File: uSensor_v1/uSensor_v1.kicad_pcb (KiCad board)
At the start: 2 copper layers, 137.6 x 77.4 mm, 287 parts, among them J1 +12V Supply, J2 Conn_01x03, J3 Conn_01x03, J4 NS25-W8P 6-pin 2,54mm, J5 USB_B, J6 GNDA-GNDD Jumper, J7 Barrel_Jack_Switch, Q1 BC817-25, Q2 BC817-25, Q3 BC847PN-7-F, Q4 BC847PN-7-F, SW1 SW_Push, SW2 SW_Push, SW3 SW_Push, U1 AM10TW-2405DZ, U10 KSS-213 Connector, U11 AD7795, U12 AD5667, U13 TBD, U14 TBD, U15 REF192, U16 TBD, U17 TBD, U2 LD1117A, U22 RCLAMP, U3 STM32F407VGTx, U4 MCP9700AT, U5 MCP9700AT, U6 LM6132A, U7 MCP9700AT, U8 MCP9700AT, U9 UG-2864KSWLG01

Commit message: Layout correction in progress.
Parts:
- added L5: 10u, Inductor_SMD:L_1210_3225Metric_Pad1.42x2.65mm_HandSolder, F.Cu at (46.9, 45.9)
- added L6: 10u, Inductor_SMD:L_1210_3225Metric_Pad1.42x2.65mm_HandSolder, F.Cu at (5.04, 47.6)
- J4: value NS25-W8P 6-pin 2,54mm -> NS25-W8P 8-pin 2,54mm; footprint Connector_Molex:Molex_KK-254_AE-6410-06A_1x06_P2.54mm_Vertical -> Connector_Molex:Molex_KK-254_AE-6410-08A_1x08_P2.54mm_Vertical
- moved C18 28.7 mm to (24.6, 35.2), turned to 90 degrees
- moved TP96 10.3 mm to (54.2, 37.2)
- moved R75 4.87 mm to (24.6, 39.0)
- moved C17 2.38 mm to (45.2, 60.6), turned to 270 degrees
- moved J4 2.32 mm to (17.1, 65.9)
- moved J5 2.00 mm to (28.5, 77.8)
- moved TP97 1.84 mm to (21.2, 33.8)
- moved C3 1.80 mm to (22.5, 45.3), turned to 270 degrees
- moved C2 1.80 mm to (16.1, 33.0)
- moved U2 1.80 mm to (17.5, 40.2)
- moved C5 1.66 mm to (45.2, 53.4), turned to 270 degrees
- moved C16 1.42 mm to (45.2, 49.2), turned to 270 degrees
- moved C4 1.35 mm to (45.2, 57.0), turned to 270 degrees
- moved C7 1.27 mm to (27.2, 44.4), turned to 180 degrees
- moved C6 1.27 mm to (40.6, 44.4), turned to 0 degrees
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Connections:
- C16 pad 1: +3V3 -> Net-(C16-Pad1)
- C16 pad 2: GNDD -> GNDA
- C38 pad 1: +3V3 -> Net-(C38-Pad1)
- C38 pad 2: GNDD -> GNDA
- C39 pad 1: +3V3 -> Net-(C38-Pad1)
- C39 pad 2: GNDD -> GNDA
- R71 pad 1: GNDD -> GNDA
- U12 pad 3: GNDD -> GNDA
- U12 pad 9: +3V3 -> Net-(C38-Pad1)
- U3 pad 20: GNDD -> GNDA
- U3 pad 22: +3V3 -> Net-(C16-Pad1)
- U3 pad 55: Net-(U3-Pad55) -> UC_DEBUG_TX
- U3 pad 56: Net-(U3-Pad56) -> UC_DEBUG_RX
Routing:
- net +3V3: track 272.1 -> 352.0 mm, vias 22 -> 14
- net GNDA: track 25.4 -> 0.00 mm, vias 0 -> 8
- net UC_DEBUG_TX: track 0.00 -> 11.0 mm
- net UC_DEBUG_RX: track 0.00 -> 10.1 mm
- net USB_VBUS: track 29.9 -> 21.3 mm
- net Net-(C16-Pad1): track 0.00 -> 6.69 mm
- net +5V: track 539.2 -> 545.0 mm
- net Net-(J5-Pad2): track 4.03 -> 0.11 mm
- net DAC_~LDAC: track 85.9 -> 82.8 mm
- net DAC_SCL: track 59.0 -> 56.3 mm
- net Net-(J5-Pad3): track 10.5 -> 8.50 mm
- net DAC_SDA: track 57.8 -> 55.8 mm
- net LCD_SCK: track 68.7 -> 70.3 mm
- net LCD_CS: track 73.0 -> 74.6 mm
- net LCD_A0: track 71.1 -> 72.7 mm
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
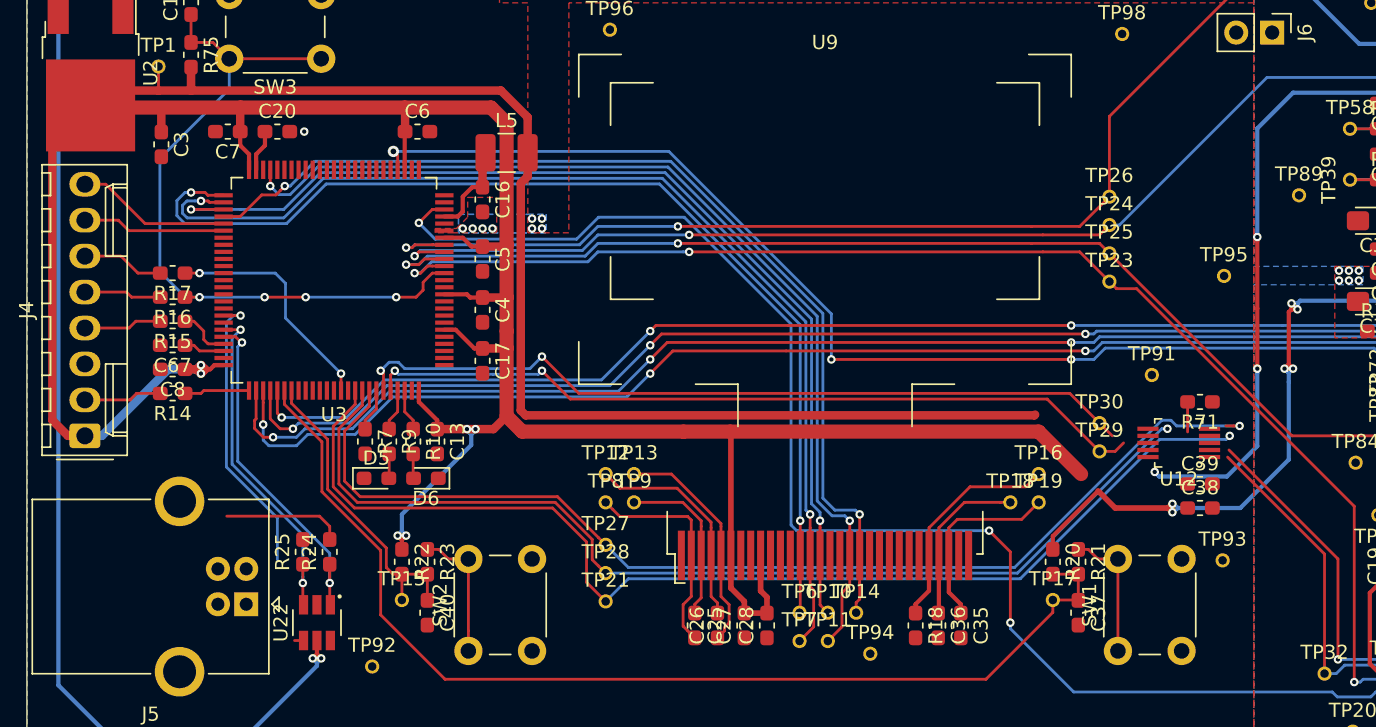
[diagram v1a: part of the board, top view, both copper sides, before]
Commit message: Layout in progress: before DAC connection changing.
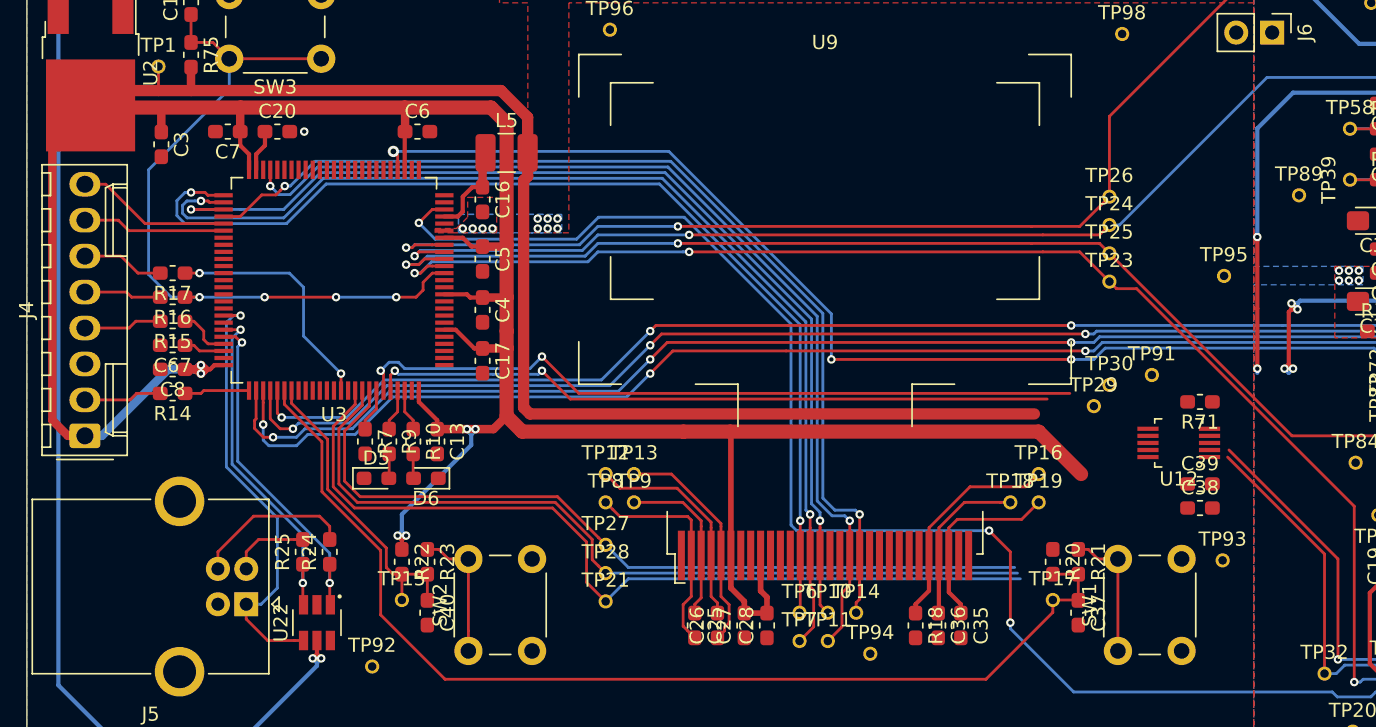
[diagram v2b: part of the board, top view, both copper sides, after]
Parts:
- moved TP29 3.22 mm to (88.4, 63.8)
- moved TP30 2.79 mm to (89.5, 62.3)
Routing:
- net +3V3: track 352.0 -> 322.2 mm, vias 14 -> 12
- net DAC_~CLR: track 78.4 -> 57.0 mm, vias 1 -> 0
- net DAC_~LDAC: track 82.8 -> 61.7 mm, vias 1 -> 0
- net DAC_ADDR: track 73.5 -> 58.7 mm, vias 1 -> 0
- net REF_2.5V: track 177.5 -> 164.1 mm, vias 4 -> 3
- net USB_VBUS: track 21.3 -> 31.0 mm
- net DAC_SDA: track 55.8 -> 48.7 mm
- net Net-(J5-Pad2): track 0.11 -> 5.67 mm
- net DAC_SCL: track 56.3 -> 52.0 mm
- net Net-(J5-Pad3): track 8.50 -> 11.4 mm
- net PROG_~RST: track 51.6 -> 52.9 mm
- net PROG_SWO: track 16.6 -> 17.2 mm
- net GNDA: vias 8 -> 10

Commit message: Layout correction in progress.
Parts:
- moved L6 143.9 mm to (144.1, 84.8), turned to 180 degrees
- moved TP29 57.7 mm to (132.8, 100.6), turned to 90 degrees
- moved TP30 56.0 mm to (131.3, 99.5), turned to 90 degrees
- moved TP91 51.7 mm to (130.6, 96.5), turned to 90 degrees
- moved C38 46.9 mm to (140.8, 84.7), turned to 90 degrees
- moved C39 45.9 mm to (139.1, 84.7), turned to 90 degrees
- moved U12 44.2 mm to (134.1, 85.8), turned to 0 degrees
- moved R71 39.4 mm to (129.1, 84.8), turned to 270 degrees
- moved TP32 33.4 mm to (135.8, 94.9)
- moved TP20 22.1 mm to (126.8, 96.1)
- moved TP77 9.34 mm to (109.4, 78.9)
- moved TP73 6.77 mm to (118.0, 82.2)
- moved TP87 6.55 mm to (149.1, 88.9)
- moved TP21 3.00 mm to (53.9, 80.6)
- moved TP27 3.00 mm to (53.9, 76.6)
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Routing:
- net +3V3: track 322.2 -> 417.6 mm, vias 12 -> 14
- net DAC_SDA: track 48.7 -> 112.1 mm, vias 2 -> 5
- net DAC_SCL: track 52.0 -> 113.8 mm, vias 2 -> 5
- net DAC_~CLR: track 57.0 -> 112.5 mm
- net DAC_ADDR: track 58.7 -> 113.1 mm
- net DAC_~LDAC: track 61.7 -> 113.7 mm
- net DAC_OUT_COIL_F_CTRL: track 58.0 -> 14.1 mm, vias 1 -> 2
- net DAC_OUT_COIL_T_CTRL: track 62.3 -> 22.7 mm
- net REF_2.5V: track 164.1 -> 181.1 mm, vias 3 -> 0
- net Net-(C38-Pad1): track 0.00 -> 6.78 mm
- net Net-(J3-Pad3): track 15.1 -> 9.97 mm
- net Net-(R1-Pad1): track 8.28 -> 11.5 mm
- net TEMP_SENS_OUT_1: track 137.4 -> 140.1 mm, vias 4 -> 6
- net +5V: track 545.0 -> 542.4 mm
- net SENS_PD: track 75.3 -> 76.3 mm
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
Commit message: Layout in progress.
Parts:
- added Mounting_Hole: MountingHole_3.2mm_M3, MountingHole:MountingHole_3.2mm_M3, F.Cu at (95.0, 52.0)
- added Mounting_Hole: MountingHole_3.2mm_M3, MountingHole:MountingHole_3.2mm_M3, F.Cu at (42.0, 30.0)
- added Mounting_Hole: MountingHole_3.2mm_M3, MountingHole:MountingHole_3.2mm_M3, F.Cu at (15.6, 87.8)
- added Mounting_Hole: MountingHole_3.2mm_M3, MountingHole:MountingHole_3.2mm_M3, F.Cu at (148.0, 15.6)
- added Mounting_Hole: MountingHole_3.2mm_M3, MountingHole:MountingHole_3.2mm_M3, F.Cu at (148.0, 87.8)
- moved TP29 91.3 mm to (50.7, 60.6), turned to 270 degrees
- moved TP30 91.1 mm to (49.7, 58.9), turned to 270 degrees
- moved TP91 86.4 mm to (44.8, 86.4)
- moved TP20 13.3 mm to (126.8, 82.8)
- moved TP32 12.8 mm to (131.1, 83.0)
- moved TP87 4.55 mm to (148.2, 84.5)
- moved C2 1.50 mm to (17.6, 33.0)
- moved TP95 1.26 mm to (97.8, 55.9)
- moved TP59 0.50 mm to (144.0, 17.4)
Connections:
- TP21 pad 1: DAC_~LDAC -> DAC_ADDR
- TP27 pad 1: DAC_~CLR -> DAC_~LDAC
- TP28 pad 1: DAC_ADDR -> DAC_~CLR
- U3 pad 91: DAC_~LDAC -> DAC_ADDR
- U3 pad 92: DAC_ADDR -> DAC_~CLR
- U3 pad 93: DAC_~CLR -> DAC_~LDAC
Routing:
- net DAC_SCL: track 113.8 -> 136.7 mm
- net +3V3: track 417.6 -> 438.3 mm
- net DAC_SDA: track 112.1 -> 130.6 mm
- net REF_2.5V: track 181.1 -> 192.9 mm, vias 0 -> 2
- net DAC_ADDR: track 113.1 -> 121.7 mm, vias 0 -> 1
- net -5V: track 214.8 -> 219.9 mm, vias 22 -> 21
- net +5V: track 542.4 -> 537.5 mm
- net DAC_~CLR: track 112.5 -> 116.6 mm, vias 0 -> 1
- net DAC_~LDAC: track 113.7 -> 117.6 mm, vias 0 -> 1
- net DAC_OUT_COIL_F_CTRL: track 14.1 -> 16.1 mm
- net GNDD: vias 9 -> 10
- net GNDA: vias 10 -> 14

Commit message: bEFORE CHECKLIST.
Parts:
- moved TP96 50.9 mm to (69.8, 85.6)
- moved TP98 48.3 mm to (42.1, 38.1)
- moved TP89 26.2 mm to (103.2, 75.1)
- moved TP95 15.7 mm to (91.5, 70.2)
- moved TP93 13.8 mm to (91.3, 62.4)
- moved J6 8.91 mm to (92.1, 37.8)
- moved TP97 1.21 mm to (22.2, 33.1)
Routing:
- net TEMP_SENS_OUT_4: track 84.3 -> 83.1 mm
- net GNDD: vias 10 -> 15
- net GNDA: vias 14 -> 11

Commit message: Components checked.
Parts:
- added TP22: TP, Sentisa-Connectors:TestPoint_Probe_1.0mmDiameter_0.6mmDrill, F.Cu at (47.5, 30.3)
- moved TP87 3.55 mm to (144.6, 84.3)
- moved L6 3.47 mm to (141.6, 87.2), turned to 90 degrees
- moved C38 1.27 mm to (141.7, 83.8), turned to 0 degrees
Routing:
- net +3V3: track 437.8 -> 431.1 mm
- net Net-(R6-Pad1): track 4.33 -> 6.35 mm
- net Net-(C38-Pad1): track 6.78 -> 8.13 mm

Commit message: Layout in progress (adding vias)
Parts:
- U13, U14, U16, U17: value TBD -> MCP6H02-E/SN
- moved C18 160.6 mm to (152.8, 132.1)
- moved C2 160.6 mm to (145.8, 129.8)
- moved C30 160.6 mm to (265.6, 142.3)
- moved C42 160.6 mm to (265.8, 151.4)
- moved C52 160.6 mm to (246.8, 117.7)
- moved R47 160.6 mm to (257.8, 175.3)
- moved R58 160.6 mm to (236.3, 129.4)
- moved R65 160.6 mm to (260.6, 112.9)
- moved R72 160.6 mm to (236.8, 155.3)
- moved R75 160.6 mm to (152.8, 135.8)
- moved RV2 160.6 mm to (258.8, 116.7)
- moved SW1 160.6 mm to (218.3, 177.9)
- moved TP32 160.6 mm to (259.3, 179.8)
- moved TP51 160.6 mm to (262.6, 122.4)
- moved TP55 160.6 mm to (275.3, 125.9)
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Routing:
- net Net-(R39-Pad2): track 14.0 -> 13.4 mm
- net GNDD: vias 15 -> 222
- net GNDA: vias 11 -> 259

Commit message: Layout in progress (adding vias)
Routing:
- net SENS_A: track 64.4 -> 63.4 mm
- net +5V: track 537.5 -> 538.0 mm
- net GNDD: vias 222 -> 309
- net GNDA: vias 259 -> 385
